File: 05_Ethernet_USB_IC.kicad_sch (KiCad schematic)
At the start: 40 parts, among them J2 R-RJ45R08P-C000, T1 G24P02S, U14 RTL8153-VB-CG, Y2 25MHz 18pF

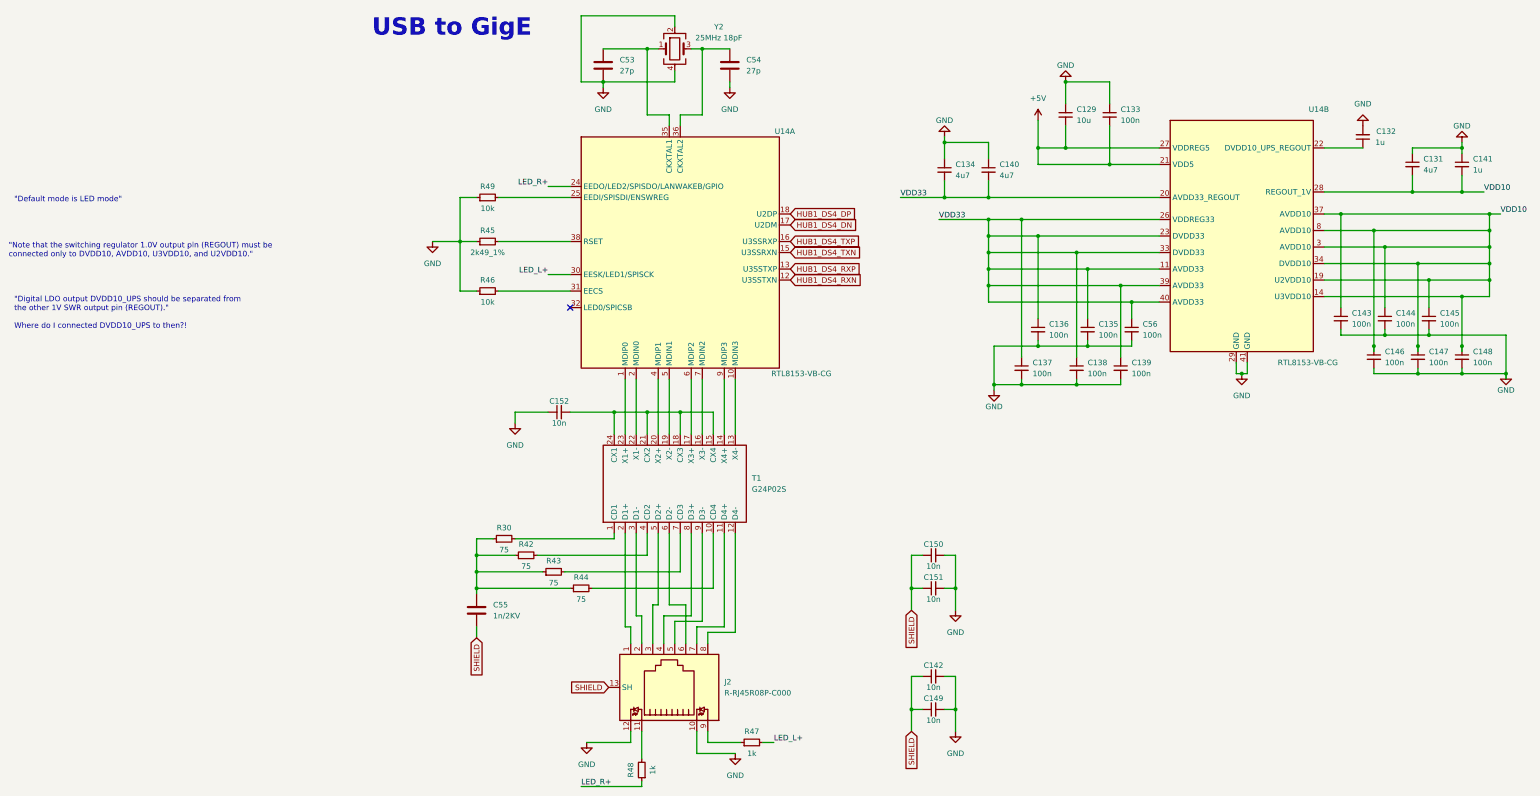
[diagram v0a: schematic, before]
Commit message: route power delivery controller
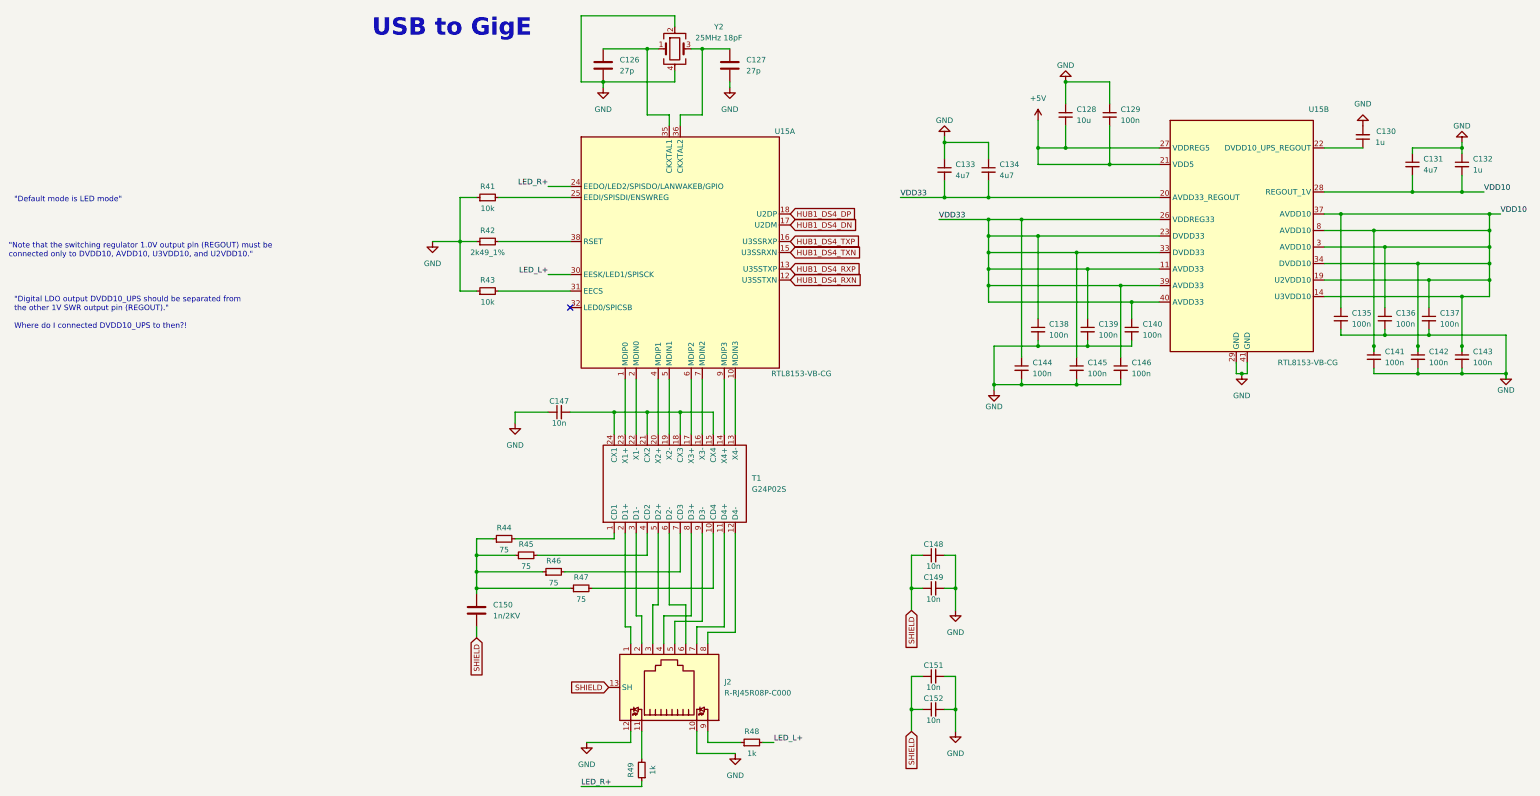
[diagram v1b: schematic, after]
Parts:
- C150: renamed from C55; footprint (none) -> Capacitor_SMD:C_0402_1005Metric
- renumbered C53 to C126, C54 to C127, C129 to C128, C133 to C129, C132 to C130, C141 to C132, C134 to C133, C140 to C134, C143 to C135, C144 to C136, C145 to C137, C136 to C138, C135 to C139, C56 to C140, C146 to C141, C147 to C142, C148 to C143, C137 to C144, C138 to C145, C139 to C146, C152 to C147, C150 to C148, C151 to C149, C142 to C151, C149 to C152, R49 to R41, R45 to R42, R46 to R43, R30 to R44, R42 to R45, R43 to R46, R44 to R47, R47 to R48, R48 to R49, U14 to U15

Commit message: settle on a layout
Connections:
- net X1+: now reaches T1.23 (X1+), U15.1 (MDIP0)
- net X4-: now reaches T1.13 (X4-), U15.10 (MDIN3)
- net X1-: now reaches T1.22 (X1-), U15.2 (MDIN0)
- net X2+: now reaches T1.20 (X2+), U15.4 (MDIP1)
- net X2-: now reaches T1.19 (X2-), U15.5 (MDIN1)
- net X3+: now reaches T1.17 (X3+), U15.6 (MDIP2)
- net X3-: now reaches T1.16 (X3-), U15.7 (MDIN2)
- net X4+: now reaches T1.14 (X4+), U15.9 (MDIP3)
- net ETH4+: now reaches J2.7, T1.11 (D4+)
- net ETH4-: now reaches J2.8, T1.12 (D4-)
- net ETH1+: now reaches J2.1, T1.2 (D1+)
- net ETH1-: now reaches J2.2, T1.3 (D1-)
- net ETH2+: now reaches J2.3, T1.5 (D2+)
- net ETH2-: now reaches J2.6, T1.6 (D2-)
- net ETH3+: now reaches J2.4, T1.8 (D3+)
- net ETH3-: now reaches J2.5, T1.9 (D3-)

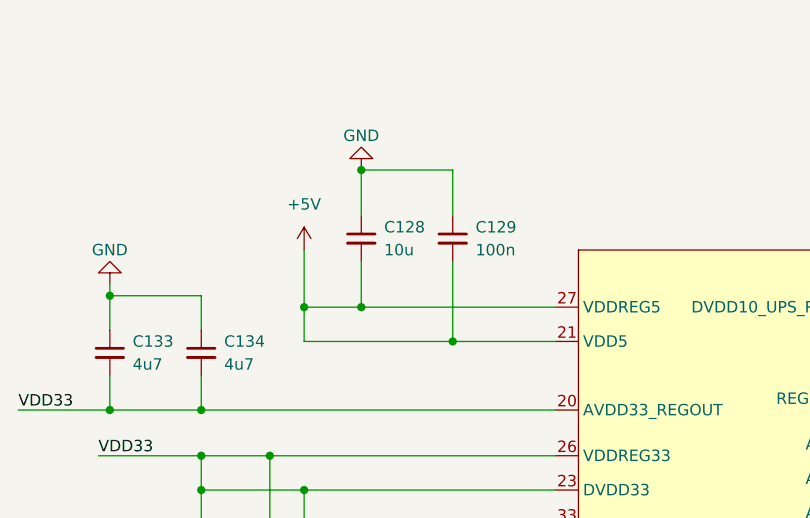
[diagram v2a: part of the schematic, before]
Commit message: power layout for ethernet usb nic
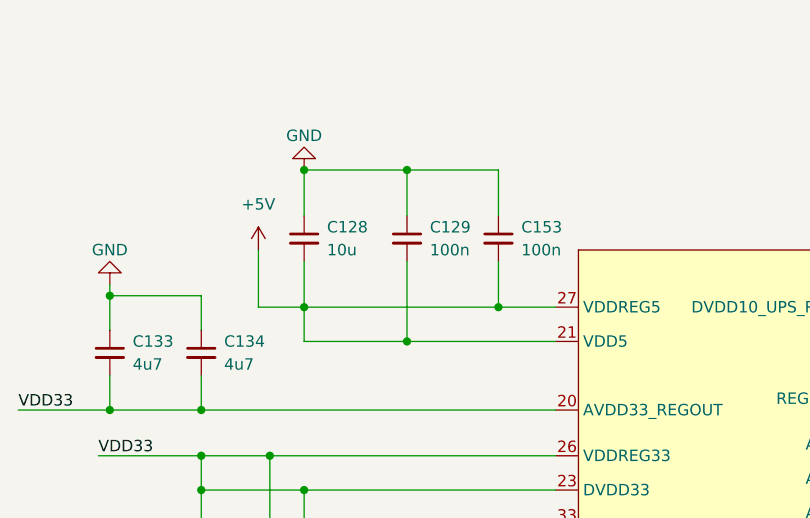
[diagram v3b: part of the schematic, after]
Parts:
- added C153: 100n, Capacitor_SMD:C_0402_1005Metric, symbol Device:C_Small
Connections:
- net +5V: now also C153.2
- net GND: now also C153.1
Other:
- moved on the sheet: C128, C129

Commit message: finish bom list
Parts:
- removed J2: R-RJ45R08P-C000, CakeUSB:R-RJ45R08P-C000, symbol CakeUSB:R-RJ45R08P-C000
- added J2: RC01931, CakeUSB:RC01931, symbol CakeUSB:RC01931
- C150: footprint Capacitor_SMD:C_0402_1005Metric -> Capacitor_SMD:C_1206_3216Metric
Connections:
- net ETH1+: now also J2.1
- net ETH1-: now also J2.2
- net ETH2+: now also J2.3
- net ETH2-: now also J2.6
- net ETH3+: now also J2.4
- net ETH3-: now also J2.5
- net ETH4+: now also J2.7
- net ETH4-: now also J2.8
- net GND: now also J2.10, J2.12
- net SHIELD: now also J2.13 (SH)
- net at R48.1: now also J2.9
- net at R49.2: now also J2.11
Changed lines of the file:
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@@
+    )
+  )
+  (symbol (lib_id "CakeUSB:RC01931") (at 82.55 170.18 270) (mirror x) (unit 1)
+    (in_bom yes) (on_board yes) (dnp no)
+    (property "Reference" "J2" (at 95.25 168.91 90)
+      (effects (font (size 1.27 1.27)) (justify left))
+    )
+    (property "Value" "RC01931" (at 95.25 171.45 90)
+      (effects (font (size 1.27 1.27)) (justify left))
+    )
+    (property "Footprint" "CakeUSB:RC01931" (at 82.55 170.18 0)
+      (effects (font (size 1.27 1.27)) hide)
+    )
+    (property "Datasheet" "" (at 82.55 170.18 0)
+      (effects (font (size 1.27 1.27)) hide)
+    )
+    (pin "9")
+    (pin "8")
+    (pin "4")
+    (pin "12")
+    (pin "11")
+    (pin "6")
+    (pin "10")
+    (pin "2")
+    (pin "1")
+    (pin "13")
+    (pin "5")
+    (pin "3")
+    (pin "7")
+    (instances
+      (project "USBHUB"
+        (path "/d5edc647-9ac3-4ac1-ab8a-57c77be3f4d3/e5ff48c6-4ab4-44af-a471-2f3943b300c6"
+          (reference "J2") (unit 1)
+        )
+      )
     )
   )
@@
       (effects (font (size 1.27 1.27)) (justify left))
     )
-    (property "Footprint" "Capacitor_SMD:C_0402_1005Metric" (at 39.0652 156.21 0)
+    (property "Footprint" "Capacitor_SMD:C_1206_3216Metric" (at 39.0652 156.21 0)
       (effects (font (size 1.27 1.27)) hide)
     )
@@
         )
       )
-    )
-  )
-  (symbol (lib_id "CakeUSB:R-RJ45R08P-C000") (at 82.55 170.18 270) (mirror x) (unit 1)
-    (in_bom yes) (on_board yes) (dnp no)
-    (property "Reference" "J2" (at 95.25 168.91 90)
-      (effects (font (size 1.27 1.27)) (justify left))
-    )
-    (property "Value" "R-RJ45R08P-C000" (at 95.25 171.45 90)
-      (effects (font (size 1.27 1.27)) (justify left))
-    )
-    (property "Footprint" "CakeUSB:R-RJ45R08P-C000" (at 91.44 168.91 0)
-      (effects (font (size 1.27 1.27)) hide)
-    )
-    (property "Datasheet" "" (at 91.44 168.91 0)
-      (effects (font (size 1.27 1.27)) hide)
-    )
-    (pin "9")
-    (pin "2")
-    (pin "3")
-    (pin "5")
-    (pin "12")
-    (pin "8")
-    (pin "1")
-    (pin "11")
-    (pin "10")
-    (pin "7")
-    (pin "13")
-    (pin "4")
-    (pin "6")
-    (instances
-      (project "USBHUB"
-        (path "/d5edc647-9ac3-4ac1-ab8a-57c77be3f4d3/e5ff48c6-4ab4-44af-a471-2f3943b300c6"
-          (reference "J2") (unit 1)
-        )
-      )
